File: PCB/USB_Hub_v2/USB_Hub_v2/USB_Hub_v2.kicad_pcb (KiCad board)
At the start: 2 copper layers, 63.2 x 106.8 mm, 83 parts, among them J1 USB_A, J2 USB_A, J3 USB_A, J4 USB_A, J5 USB_A, J6 USB_A, SW1 SW_Push_DPDT, U1 FE1.1s, U2 TS3USB30EDGSR, U3 TPS2116DRL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

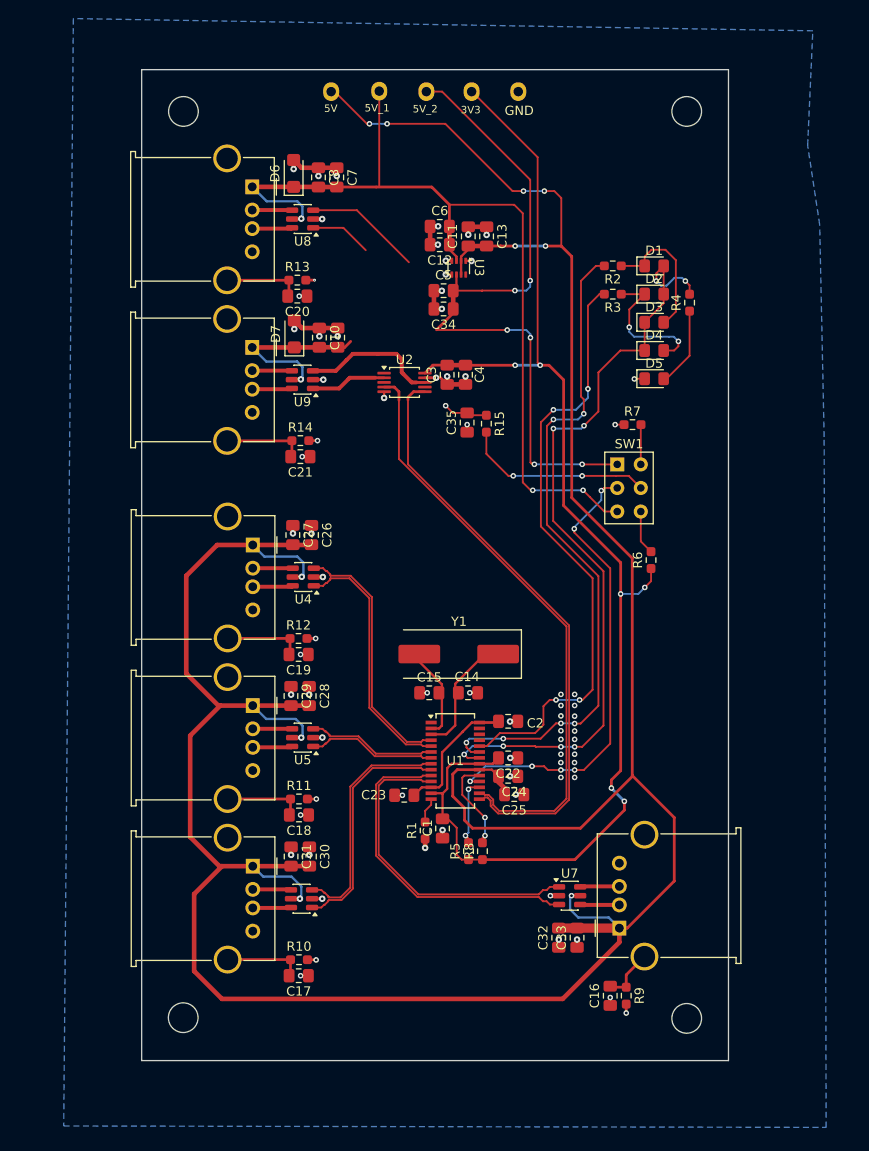
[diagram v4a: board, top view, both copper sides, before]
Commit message: Rev 2 finished
Updated layout and added parts to improve next version
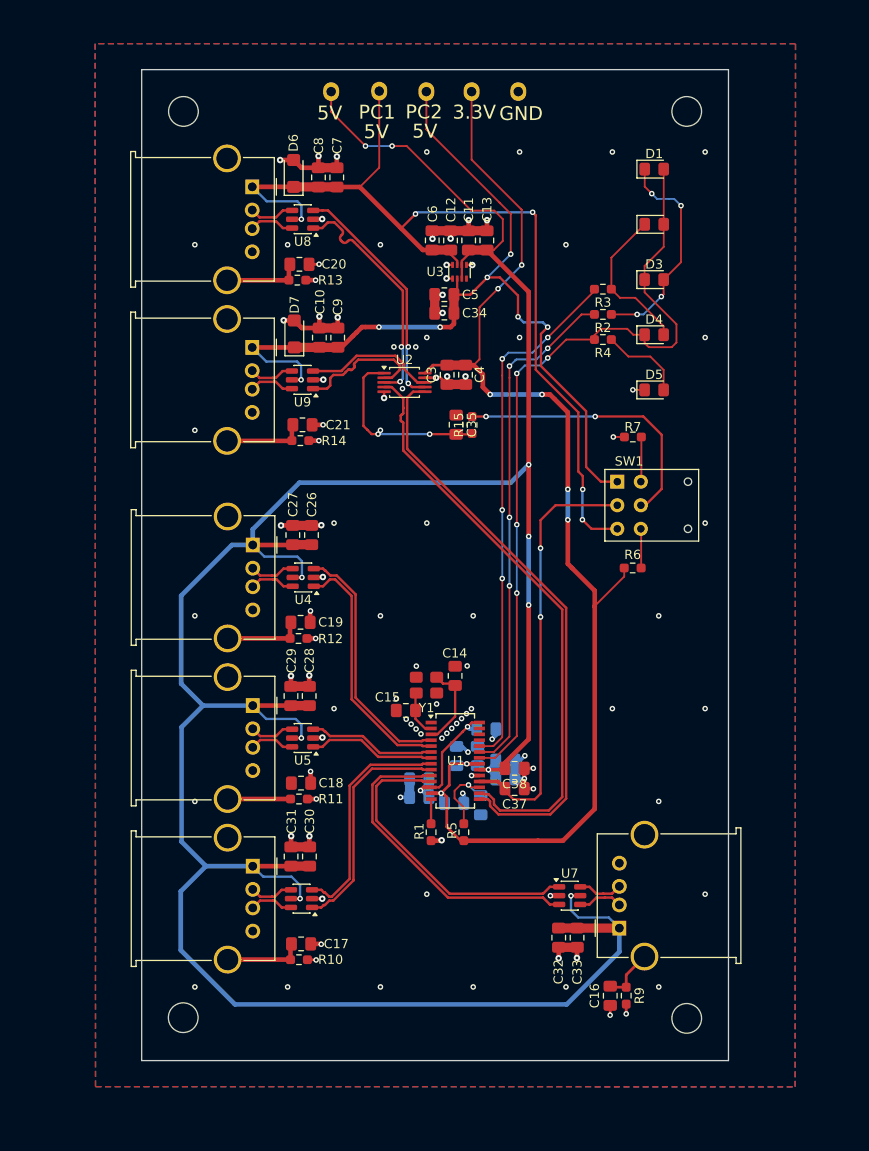
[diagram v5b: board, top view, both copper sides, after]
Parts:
- removed R8: 10k, Resistor_SMD:R_0603_1608Metric_Pad0.98x0.95mm_HandSolder
- added C36: 100n, Capacitor_SMD:C_0805_2012Metric_Pad1.18x1.45mm_HandSolder, B.Cu at (77.7, 115.3)
- added C37: 100n, Capacitor_SMD:C_0805_2012Metric_Pad1.18x1.45mm_HandSolder, F.Cu at (81.3, 113.5)
- added C38: 10u, Capacitor_SMD:C_0805_2012Metric_Pad1.18x1.45mm_HandSolder, F.Cu at (81.3, 111.3)
- added C39: 100n, Capacitor_SMD:C_0805_2012Metric_Pad1.18x1.45mm_HandSolder, B.Cu at (75.1, 110.0)
- added C40: 100n, Capacitor_SMD:C_0805_2012Metric_Pad1.18x1.45mm_HandSolder, B.Cu at (78.3, 107.1)
- C1, C2, C22, C23, C24, C25: moved to B.Cu
- R1: value 2.7k -> 2.7k 1%
- Y1: footprint Crystal:Crystal_SMD_HC49-SD -> Crystal:Crystal_SMD_3225-4Pin_3.2x2.5mm
- moved C2 11.4 mm to (71.1, 112.5), turned to 0 degrees
- moved D1 10.4 mm to (96.4, 46.7)
- moved R4 10.2 mm to (90.9, 65.1), turned to 180 degrees
- moved C1 8.68 mm to (77.3, 110.0), turned to -90 degrees
- moved C22 7.60 mm to (74.8, 115.1)
- moved D2 7.52 mm to (96.4, 52.7)
- moved R2 5.34 mm to (90.9, 62.4)
- moved Y1 4.83 mm to (71.8, 102.3)
- moved D3 4.60 mm to (96.4, 58.6)
- moved C25 3.81 mm to (80.3, 110.4)
- moved C19 3.47 mm to (58.3, 95.6)
- moved C18 3.44 mm to (58.3, 112.9)
- moved C17 3.44 mm to (58.3, 130.2)
- moved C21 3.44 mm to (58.5, 74.3)
- moved C20 3.44 mm to (58.1, 57.0)
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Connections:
- net Net-(U1-~{XRSTJ}) renamed XRSTJ
- U1 pad 19: Net-(U1-BUSJ) -> GND
- Y1 pad 2: Net-(U1-XOUT) -> GND
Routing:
- net GND: track 70.0 -> 96.0 mm, vias 73 -> 107
- net /5V: track 338.8 -> 316.2 mm
- net /DPC1+: track 6.66 -> 25.9 mm, vias 0 -> 2
- net /LED1: track 72.7 -> 55.3 mm, vias 6 -> 4
- net Net-(U2-S): track 4.81 -> 19.8 mm, vias 1 -> 3
- net /DPC1-: track 12.6 -> 25.9 mm, vias 0 -> 2
- net Net-(U1-BUSJ): track 10.1 -> 0.00 mm, vias 2 -> 0
- net /S_TS3USB: track 20.5 -> 30.1 mm
- net /5V_1: track 96.2 -> 105.5 mm, vias 3 -> 5
- net /LED2: track 65.4 -> 56.8 mm
- net Net-(D1-K): track 15.0 -> 23.5 mm, vias 0 -> 4
- net /3.3V: track 141.9 -> 135.1 mm, vias 6 -> 8
- net /5V_2: track 95.1 -> 101.8 mm
- net /DPC2+: track 8.14 -> 14.2 mm
- net Net-(J2-Shield): track 12.6 -> 6.78 mm
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- added copper zone on F.Cu, net GND
- added copper zone on In1.Cu, net GND
- added copper zone on In2.Cu, net GND
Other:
- copper layers 2 -> 4
- board text added: "1"
- board text added: "2"
- board text added: "5V"
